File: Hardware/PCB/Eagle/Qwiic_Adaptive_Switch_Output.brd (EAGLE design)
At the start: 43.2 x 38.1 mm, 61 parts, among them J1 QWIIC_RIGHT_ANGLE, J4 QWIIC_RIGHT_ANGLE, K1 G3VM-41DY1, K2 G3VM-41DY1, SW1 CUI_SJ1-3513, SW2 CUI_SJ1-3513, U1 TCA9534

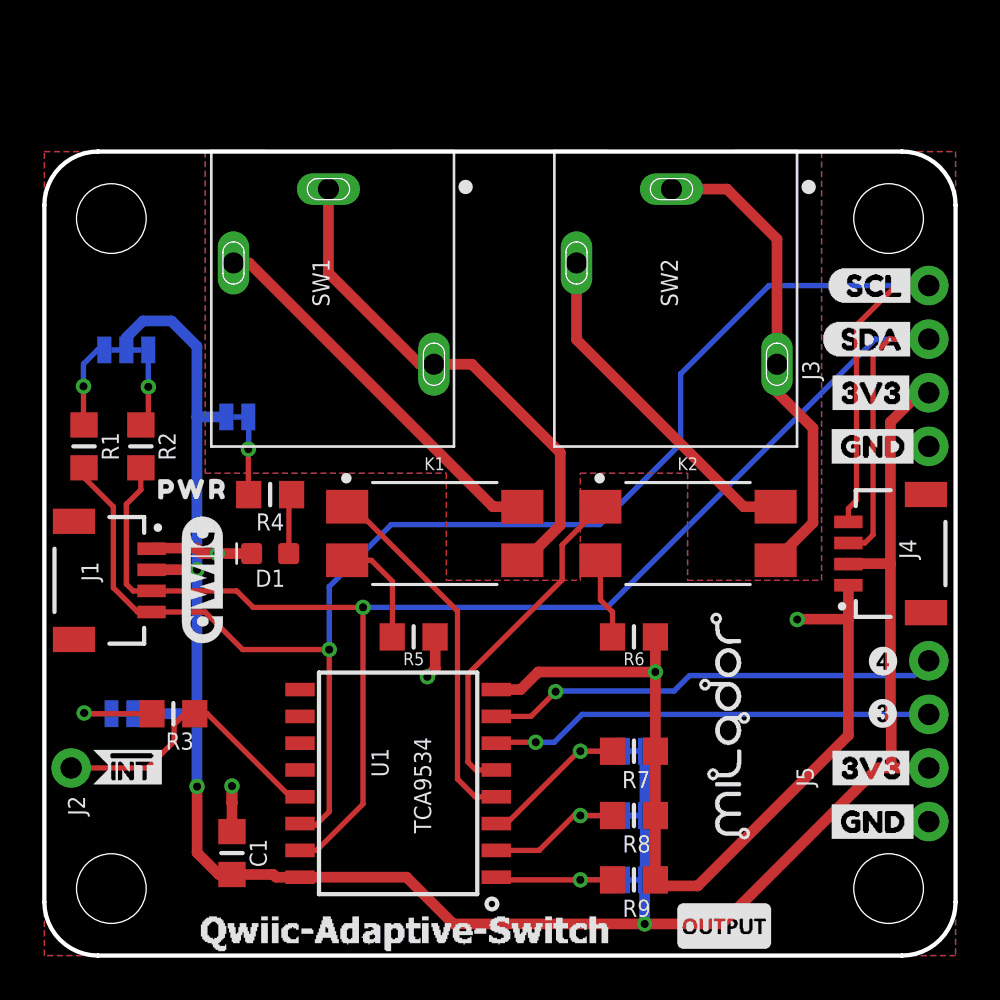
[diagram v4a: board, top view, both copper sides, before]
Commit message: Updated silkscreen
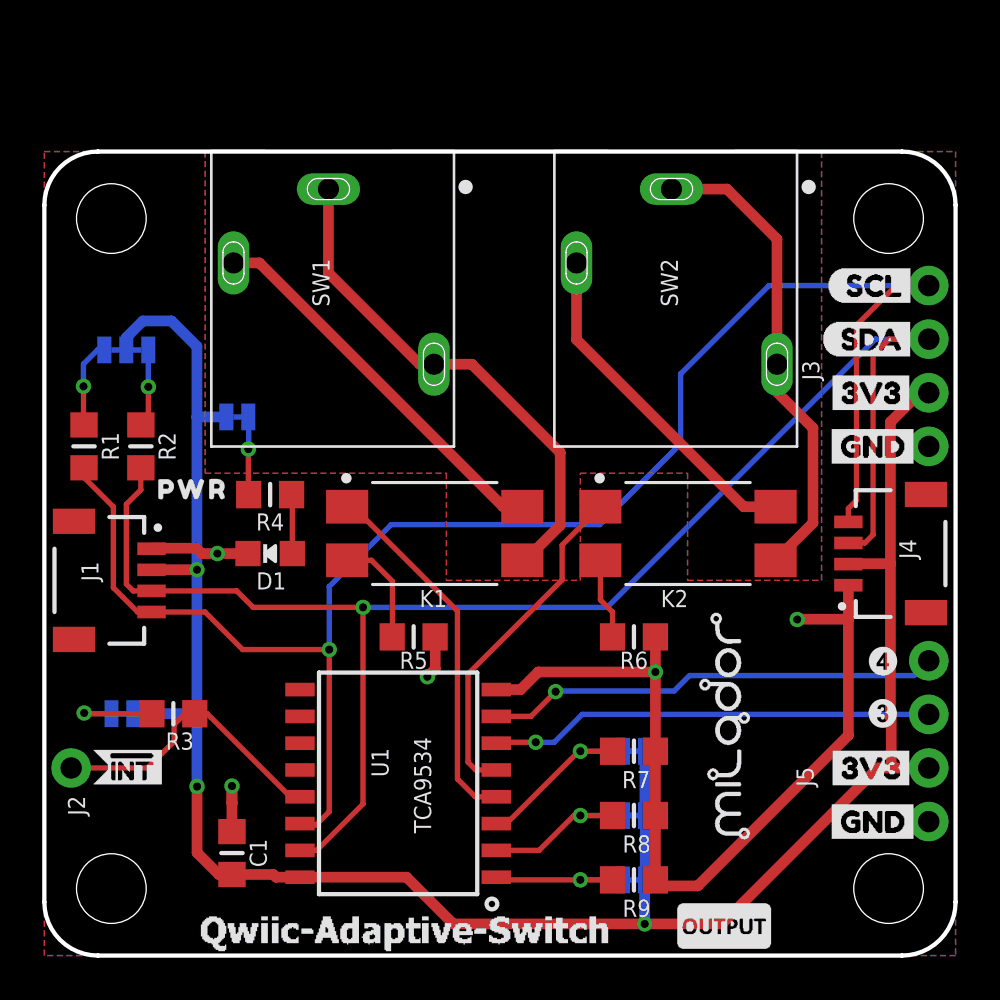
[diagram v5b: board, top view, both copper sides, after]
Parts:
- removed LABEL_6: (no value), SparkFun-Aesthetics:QWIIC_6MM
- D1: device milador_SMD:LED-0603 -> milador_SMD:CHIPLED_0805_NOOUTLINE
- turned D1 to 90 degrees

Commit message: Updated design to version 1.2
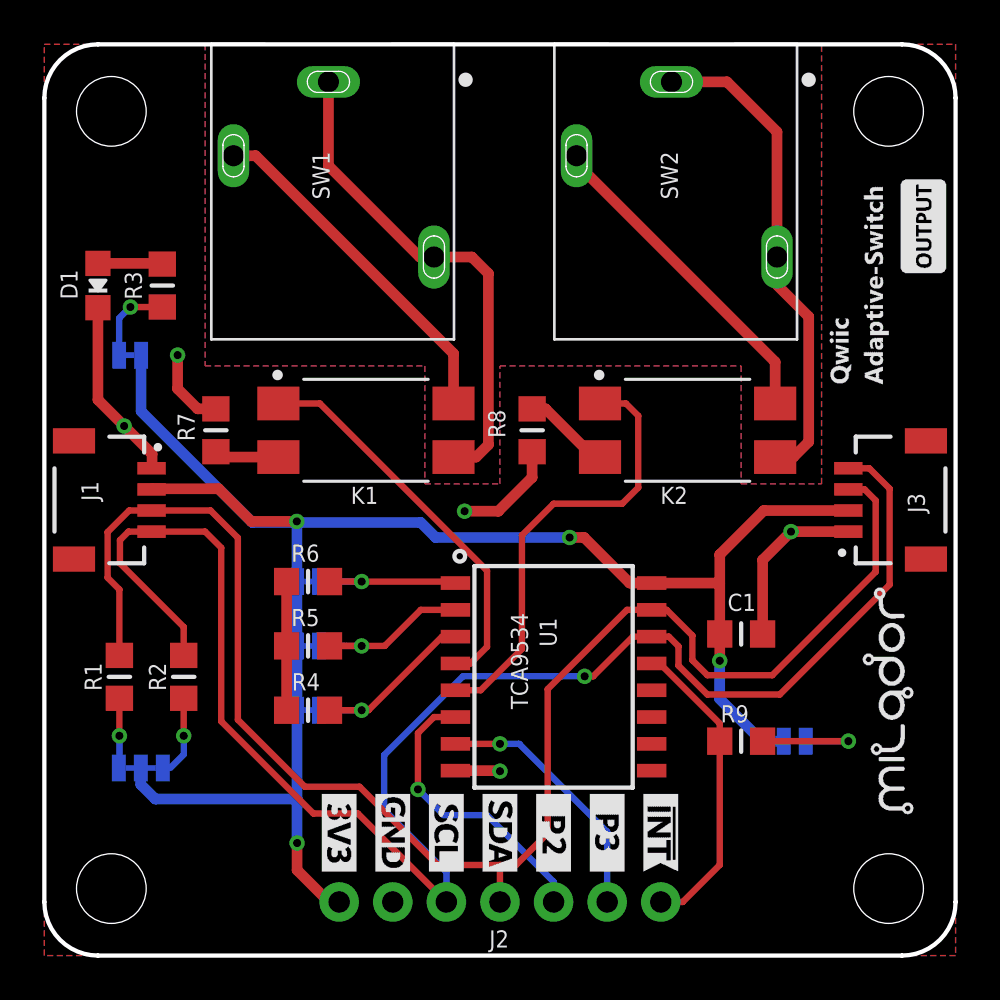
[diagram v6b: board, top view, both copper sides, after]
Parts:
- removed J4: QWIIC_RIGHT_ANGLE, milador_SMD:CONNECTORS_JST04_1MM_RA
- removed J5: (no value), milador:CONNECTORS_1X04_NO_SILK
- removed LABEL_1: (no value), SparkFun-Buzzard:I2C
- removed LABEL_10: (no value), output:#INT#0
- removed LABEL_11: (no value), buzzard_labels (52):#INT0
- removed LABEL_12: (no value), buzzard_labels (54):#INT0
- removed LABEL_13, LABEL_7: MILADOR-LOGO-, milador:MILADOR_LOGO1
- removed LABEL_14: (no value), output:#ADR2#0
- removed LABEL_15: (no value), output:#ADR1#0
- removed LABEL_16: (no value), output:#ADR0#0
- removed LABEL_17, LABEL_8: (no value), milador:MILADOR_QWIIC_SWITCH
- removed LABEL_18, LABEL_9: MILADOR-SWITCH-NAME-SW-OUTPUT, milador:SWITCH-OUTPUT
- removed LABEL_19: (no value), buzzard_labels (44):SCL6
- removed LABEL_2: MILADOR-SWITCH-NAME-SW1, milador:SWITCH-SW1
- removed LABEL_20: (no value), buzzard_labels (44):SDA5
- removed LABEL_21, LABEL_23, LABEL_27, LABEL_29: (no value), buzzard_labels (44):3V33
- removed LABEL_22, LABEL_24, LABEL_30, U$28: (no value), buzzard_labels (44):GND4
- removed LABEL_25: (no value), buzzard_labels (51):SCL0
- removed LABEL_26: (no value), buzzard_labels (51):SDA1
- removed LABEL_3: MILADOR-SWITCH-NAME-SW2, milador:SWITCH-SW2
- removed LABEL_4: (no value), output:#PWR#0
- removed LABEL_5: (no value), output:PWR0
- added LABEL_!INT_BOTTOM, LABEL_!INT_TOP: MILADOR-LABEL-!INT, milador:LABEL-!INT
- added LABEL_3V_BOTTOM, LABEL_3V_TOP: MILADOR-LABEL-3V, milador:LABEL-3V
- added LABEL_ADR0: MILADOR-LABEL-ADR0, milador:LABEL-ADR0
- added LABEL_ADR1: MILADOR-LABEL-ADR1, milador:LABEL-ADR1
- added LABEL_ADR2: MILADOR-LABEL-ADR2, milador:LABEL-ADR2
- added LABEL_GND_BOTTOM, LABEL_GND_TOP: MILADOR-LABEL-GND, milador:LABEL-GND
- added LABEL_I2C: MILADOR-LABEL-I2C, milador:LABEL-I2C
- added LABEL_I2C_ADDRESS: MILADOR-LABEL-ADDRESS-0X27, milador:LABEL-ADDRESS-27
- added LABEL_INT: MILADOR-LABEL-INT, milador:LABEL-INT
- added LABEL_MILADOR_BOTTOM, LABEL_MILADOR_TOP: MILADOR-LOGO-, milador:MILADOR_LOGO1
- added LABEL_OUTPUT_BOTTOM, LABEL_OUTPUT_TOP: MILADOR-SWITCH-NAME-SW-OUTPUT, milador:SWITCH-OUTPUT
- added LABEL_P0_BOTTOM: MILADOR-LABEL-P0, milador:LABEL-P0
- added LABEL_P1_BOTTOM: MILADOR-LABEL-P1, milador:LABEL-P1
- added LABEL_P2_BOTTOM, LABEL_P2_TOP: MILADOR-LABEL-P2, milador:LABEL-P2
- added LABEL_P3_BOTTOM, LABEL_P3_TOP: MILADOR-LABEL-P3, milador:LABEL-P3
- added LABEL_PWR: MILADOR-LABEL-PWR, milador:LABEL-PWR
- added LABEL_SW1: MILADOR-SWITCH-NAME-SW1, milador:SWITCH-SW1
- added LABEL_SW2: MILADOR-SWITCH-NAME-SW2, milador:SWITCH-SW2
- added LABEL_TITLE_BOTTOM: MILADOR-DEVICE-QWIIC-SWITCH, milador:MILADOR_QWIIC_SWITCH
- added LABEL_TITLE_TOP: MILADOR-DEVICE-QWIIC-SWITCH-SM, milador:MILADOR_QWIIC_SWITCH_SM
- added LABE_SCL_BOTTOM, LABE_SCL_TOP: MILADOR-LABEL-SCL, milador:LABEL-SCL
- added LABE_SDA_BOTTOM, LABE_SDA_TOP: MILADOR-LABEL-SDA, milador:LABEL-SDA
- J2: device milador:CONNECTORS_1X01_NO_SILK -> milador:CONNECTORS_1X07_NO_SILK
- J3: value (none) -> QWIIC_RIGHT_ANGLE; device milador:CONNECTORS_1X04_NO_SILK -> milador_SMD:CONNECTORS_JST04_1MM_RA
- R3: value 10k -> 1k
- R4: value 1k -> 2.2k
- R5, R6: value 220 -> 2.2k
- R7, R8: value 2.2k -> 220
- R9: value 2.2k -> 10k
- moved INT 31.9 mm to (35.6, 10.2), turned to 0 degrees
- moved C1 26.3 mm to (33.0, 15.2), turned to 0 degrees
- moved R7 25.0 mm to (8.13, 24.9), turned to 90 degrees
- moved ADR0 20.9 mm to (12.5, 17.7), turned to 0 degrees
- moved R3 20.3 mm to (5.59, 31.8), turned to 270 degrees
- moved I2C 19.8 mm to (4.57, 8.89), turned to 180 degrees
- moved R8 18.9 mm to (23.1, 24.9), turned to 270 degrees
- moved ADR1 17.4 mm to (12.5, 14.7), turned to 0 degrees
- moved R6 15.7 mm to (12.5, 17.7)
- moved ADR2 15.6 mm to (12.5, 11.6), turned to 0 degrees
- moved D1 15.1 mm to (2.54, 31.8), turned to 180 degrees
- moved J2 14.2 mm to (14.0, 2.54), turned to 0 degrees
- moved R2 11.1 mm to (6.60, 13.2), turned to 270 degrees
- moved R1 11.0 mm to (3.56, 13.2), turned to 270 degrees
- moved R4 10.4 mm to (12.5, 11.6), turned to 0 degrees
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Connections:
- net !INT: now also J2.7, R9.1; no longer J2.1, R3.1
- net 3.3V: now also J2.1; no longer J4.2, J5.2
- net ADR0: now also R6.2; no longer R9.2
- net ADR1: now also R5.2; no longer R8.2
- net ADR2: now also R4.2; no longer R7.2
- net GND: now also J2.2, R4.1, R5.1, R6.1, R7.2, R8.2; no longer J4.1, J5.1, R5.2, R6.2, R7.1, R8.1, R9.1
- net N$1: now also R9.2; no longer R3.2
- net N$2: now also R3.1; no longer R4.1
- net N$3: now also R3.2; no longer R4.2
- net N$5: now also R7.1; no longer R5.1
- net N$7: now also R8.1; no longer R6.1
- net P2: now also J2.5; no longer J5.3
- net P3: now also J2.6; no longer J5.4
- net SCL: now also J2.3, R2.1; no longer J4.4, R1.1
- net SCL_PU1: now also R1.2; no longer R2.2
- net SDA: now also J2.4, R1.1; no longer J4.3, R2.1
- net SDA_PU1: now also R2.2; no longer R1.2
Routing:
- net 3.3V: track 103.6 -> 86.4 mm, vias 3 -> 4
- net GND: track 50.9 -> 33.9 mm
- net P3: track 21.6 -> 12.2 mm
- net P2: track 21.1 -> 14.0 mm
- net P1: track 16.2 -> 21.3 mm
- net N$5: track 5.20 -> 3.07 mm
- net N$4: track 18.5 -> 16.7 mm
- net N$1: track 4.53 -> 6.08 mm
- net P0: track 17.4 -> 18.6 mm
- net SDA: track 75.6 -> 74.6 mm, vias 1 -> 0
- net N$6: track 24.4 -> 23.7 mm
- net N$8: track 16.3 -> 15.6 mm
- net !INT: track 14.0 -> 14.6 mm
- net N$9: track 22.6 -> 23.2 mm
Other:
- board size 43.2 x 38.1 mm -> 43.2 x 43.2 mm

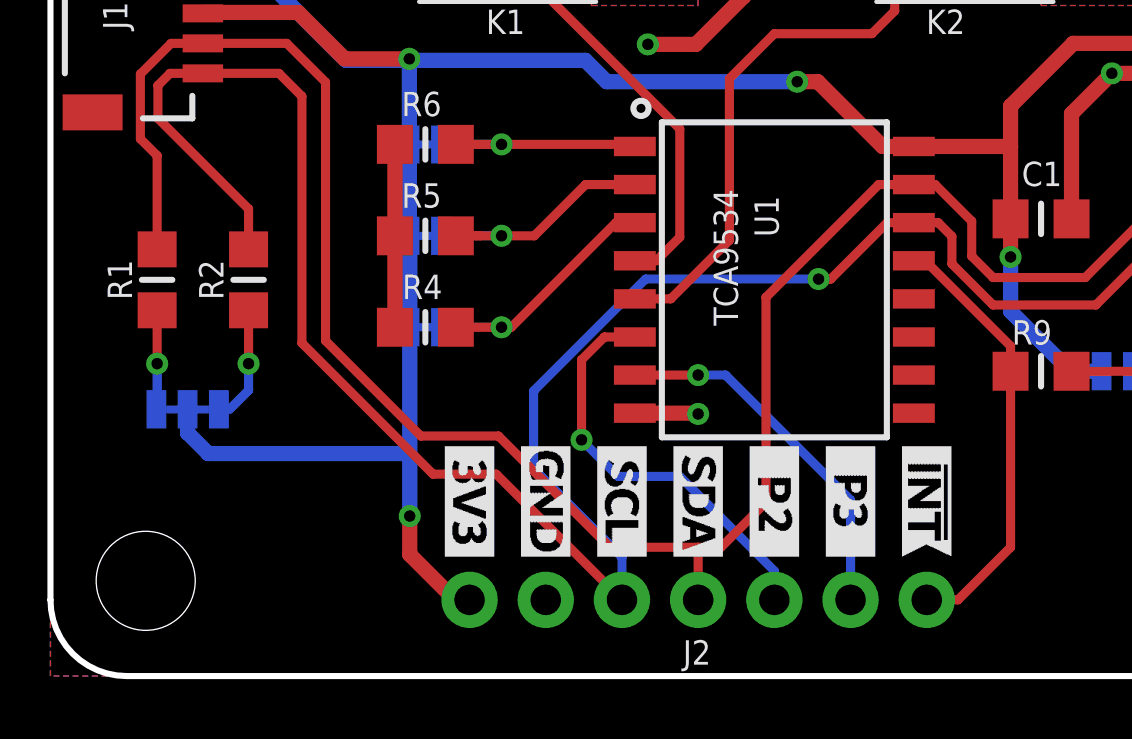
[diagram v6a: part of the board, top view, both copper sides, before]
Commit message: Updated header pin order
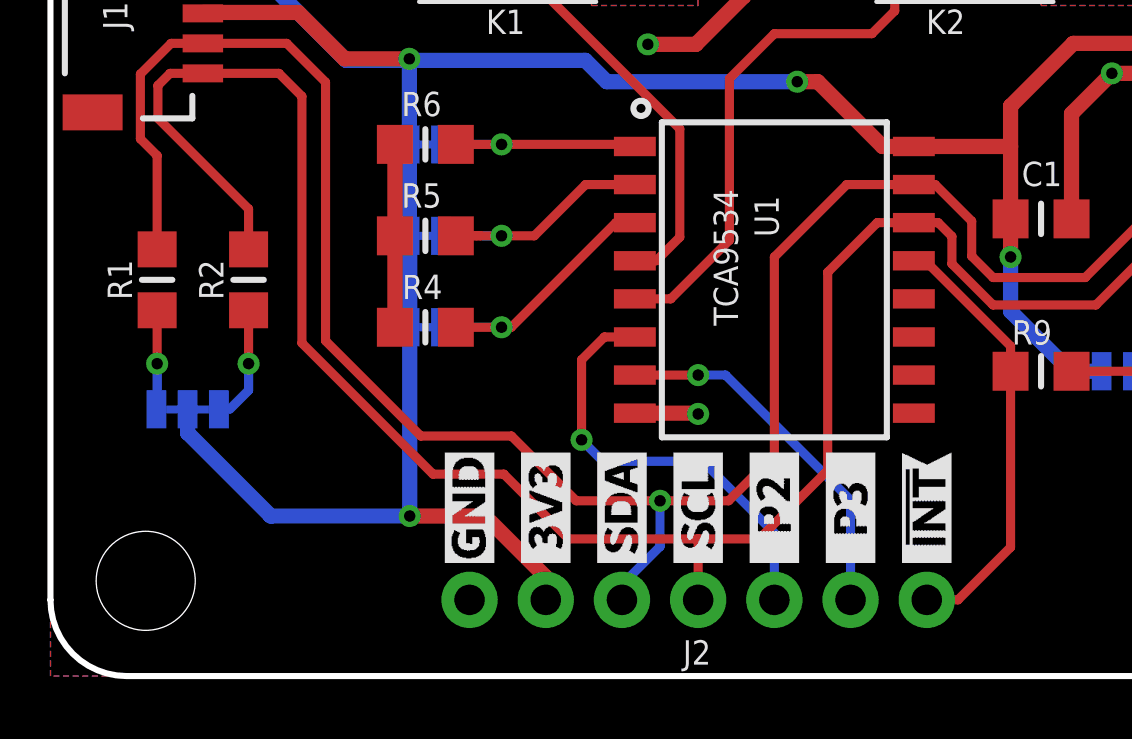
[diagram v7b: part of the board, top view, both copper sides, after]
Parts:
- removed JP3: STAND-OFF-3.3, milador:STAND-OFF-3.3
- added H3: STAND-OFF-3.3, milador:STAND-OFF-3.3
- moved H1 52.1 mm to (3.17, 3.17)
- moved LABEL_3V_TOP 4.58 mm to (16.5, 3.81), turned to 90 degrees
- moved LABEL_GND_TOP 4.58 mm to (14.0, 3.81), turned to 90 degrees
- moved LABE_SCL_TOP 4.58 mm to (21.6, 3.81), turned to 90 degrees
- moved LABE_SDA_TOP 4.58 mm to (19.1, 3.81), turned to 90 degrees
- moved LABEL_!INT_TOP 3.81 mm to (29.2, 3.81), turned to 90 degrees
- moved LABEL_P2_TOP 3.81 mm to (24.1, 3.81), turned to 90 degrees
- moved LABEL_P3_TOP 3.81 mm to (26.7, 3.81), turned to 90 degrees
- moved LABEL_3V_BOTTOM 2.54 mm to (16.5, 3.81)
- moved LABEL_GND_BOTTOM 2.54 mm to (14.0, 3.81)
- moved LABE_SCL_BOTTOM 2.54 mm to (21.6, 3.81)
- moved LABE_SDA_BOTTOM 2.54 mm to (19.1, 3.81)
- renumbered JP4 to H4
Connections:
- net 3.3V: now also J2.2; no longer J2.1
- net GND: now also J2.1; no longer J2.2
- net SCL: now also J2.4; no longer J2.3
- net SDA: now also J2.3; no longer J2.4
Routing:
- net SCL: track 79.6 -> 75.6 mm, vias 1 -> 0
- net 3.3V: track 86.4 -> 89.5 mm
- net P2: track 14.0 -> 14.7 mm
- net SDA: track 74.6 -> 75.2 mm, vias 0 -> 1
